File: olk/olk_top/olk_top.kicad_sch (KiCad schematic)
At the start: 64 parts, among them SW0 SWITCH, SW1 SWITCH, SW10 SWITCH, SW11 SWITCH, SW12 SWITCH, SW13 SWITCH, SW14 SWITCH, SW15 SWITCH, SW16 SWITCH, SW17 SWITCH, SW18 SWITCH, SW19 SWITCH, SW2 SWITCH, SW20 SWITCH, SW21 SWITCH, SW22 SWITCH, SW23 SWITCH, SW24 SWITCH, SW25 SWITCH, SW26 SWITCH, SW27 SWITCH, SW28 SWITCH, SW29 SWITCH, SW3 SWITCH, SW30 SWITCH, SW31 SWITCH, SW32 SWITCH, SW33 SWITCH, SW34 SWITCH, SW35 SWITCH, SW36 SWITCH, SW37 SWITCH, SW38 SWITCH, SW39 SWITCH, SW4 SWITCH, SW40 SWITCH, SW41 SWITCH, SW42 SWITCH, SW43 SWITCH, SW44 SWITCH, SW45 SWITCH, SW46 SWITCH, SW47 SWITCH, SW48 SWITCH, SW49 SWITCH, SW5 SWITCH, SW50 SWITCH, SW51 SWITCH, SW52 SWITCH, SW53 SWITCH, SW54 SWITCH, SW55 SWITCH, SW6 SWITCH, SW7 SWITCH, SW8 SWITCH, SW9 SWITCH

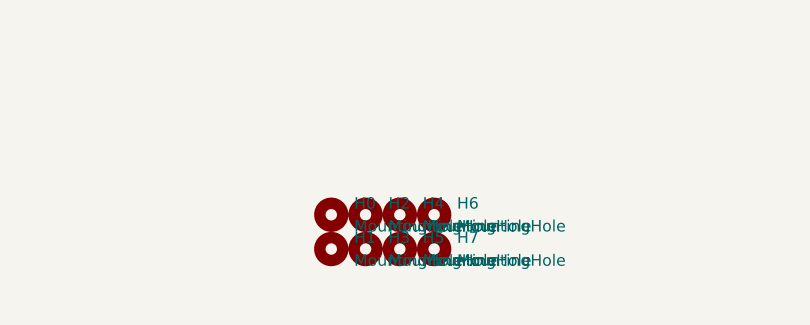
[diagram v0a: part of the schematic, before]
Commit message: Updated the top shape to match the pcb.
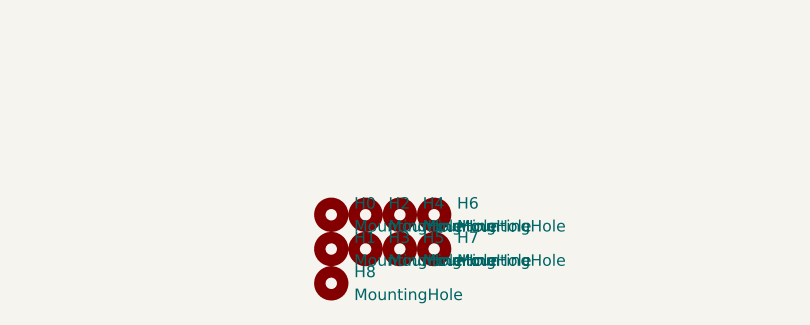
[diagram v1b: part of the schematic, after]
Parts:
- added H8: MountingHole, MountingHole:MountingHole_2.2mm_M2_ISO7380_Pad, symbol Mechanical:MountingHole
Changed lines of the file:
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@@
+	)
+	(symbol
+		(lib_id "Mechanical:MountingHole")
+		(at 119.38 257.81 0)
+		(unit 1)
+		(body_style 1)
+		(exclude_from_sim no)
+		(in_bom yes)
+		(on_board yes)
+		(in_pos_files yes)
+		(dnp no)
+		(fields_autoplaced yes)
+		(property "Reference" "H8"
+			(at 121.92 256.54 0)
+			(show_name no)
+			(do_not_autoplace no)
+			(effects
+				(font
+					(size 1.27 1.27)
+				)
+				(justify left)
+			)
+		)
+		(property "Value" "MountingHole"
+			(at 121.92 259.08 0)
+			(show_name no)
+			(do_not_autoplace no)
+			(effects
+				(font
+					(size 1.27 1.27)
+				)
+				(justify left)
+			)
+		)
+		(property "Footprint" "MountingHole:MountingHole_2.2mm_M2_ISO7380_Pad"
+			(at 119.38 257.81 0)
+			(hide yes)
+			(show_name no)
+			(do_not_autoplace no)
+			(effects
+				(font
+					(size 1.27 1.27)
+				)
+			)
+		)
+		(property "Datasheet" ""
+			(at 119.38 257.81 0)
+			(hide yes)
+			(show_name no)
+			(do_not_autoplace no)
+			(effects
+				(font
+					(size 1.27 1.27)
+				)
+			)
+		)
+		(property "Description" ""
+			(at 119.38 257.81 0)
+			(show_name no)
+			(do_not_autoplace no)
+			(effects
+				(font
+					(size 1.27 1.27)
+				)
+			)
+		)
+		(instances
+			(project "olk_top"
+				(path "/97127b28-60f4-45ff-835e-dccfbc833331"
+					(reference "H8")
+					(unit 1)
+				)
+			)
+		)
 	)
 	(symbol

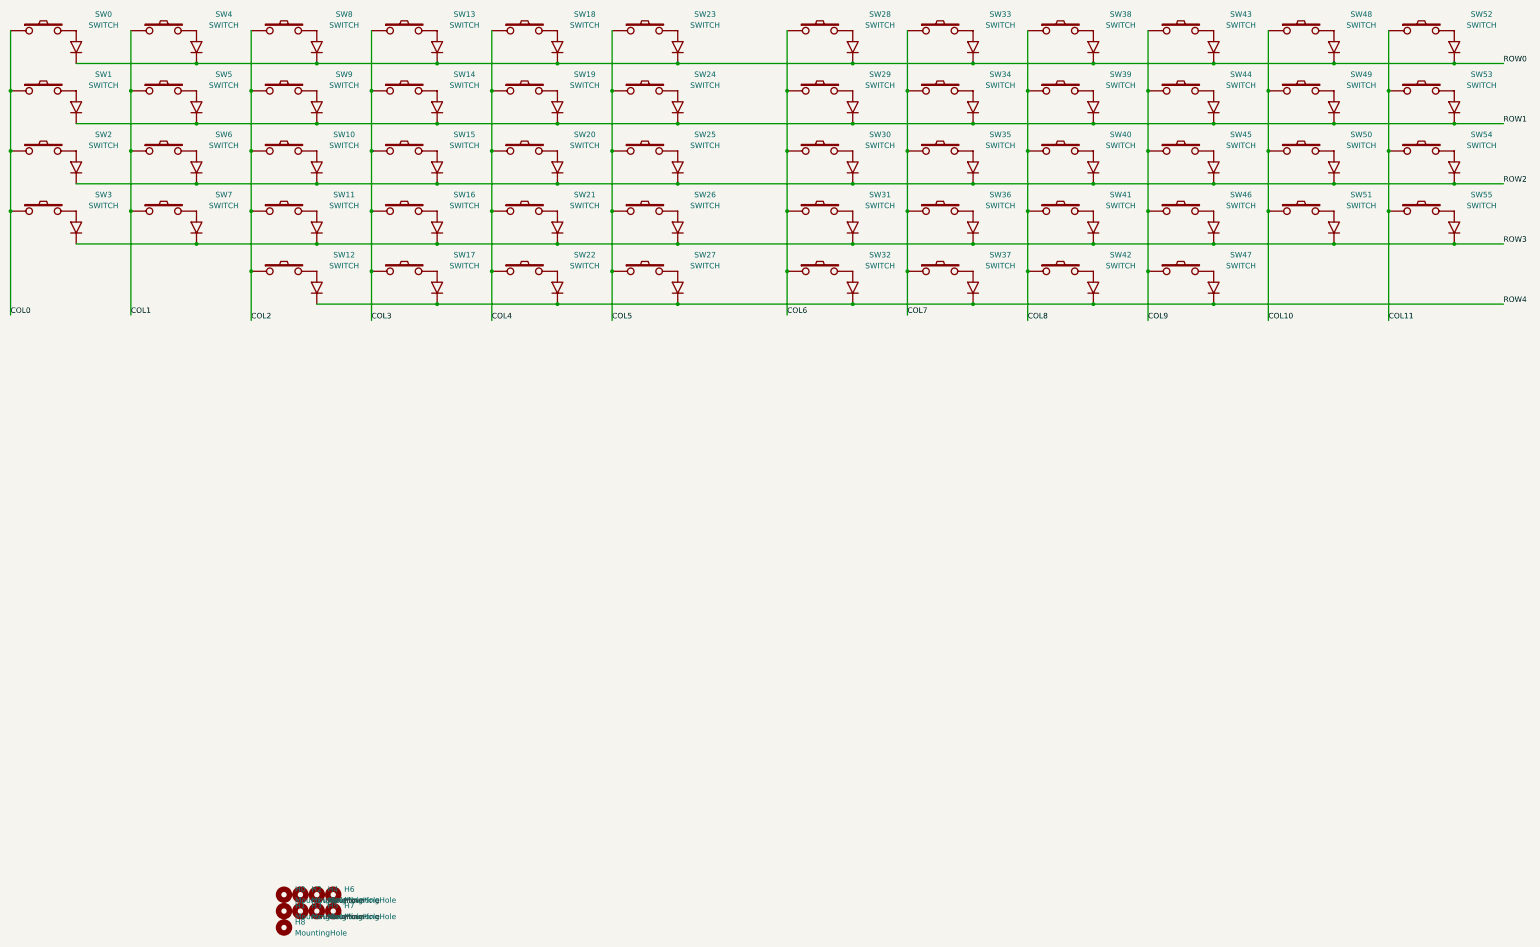
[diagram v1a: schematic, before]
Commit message: Updated olk_top to match the new layout.
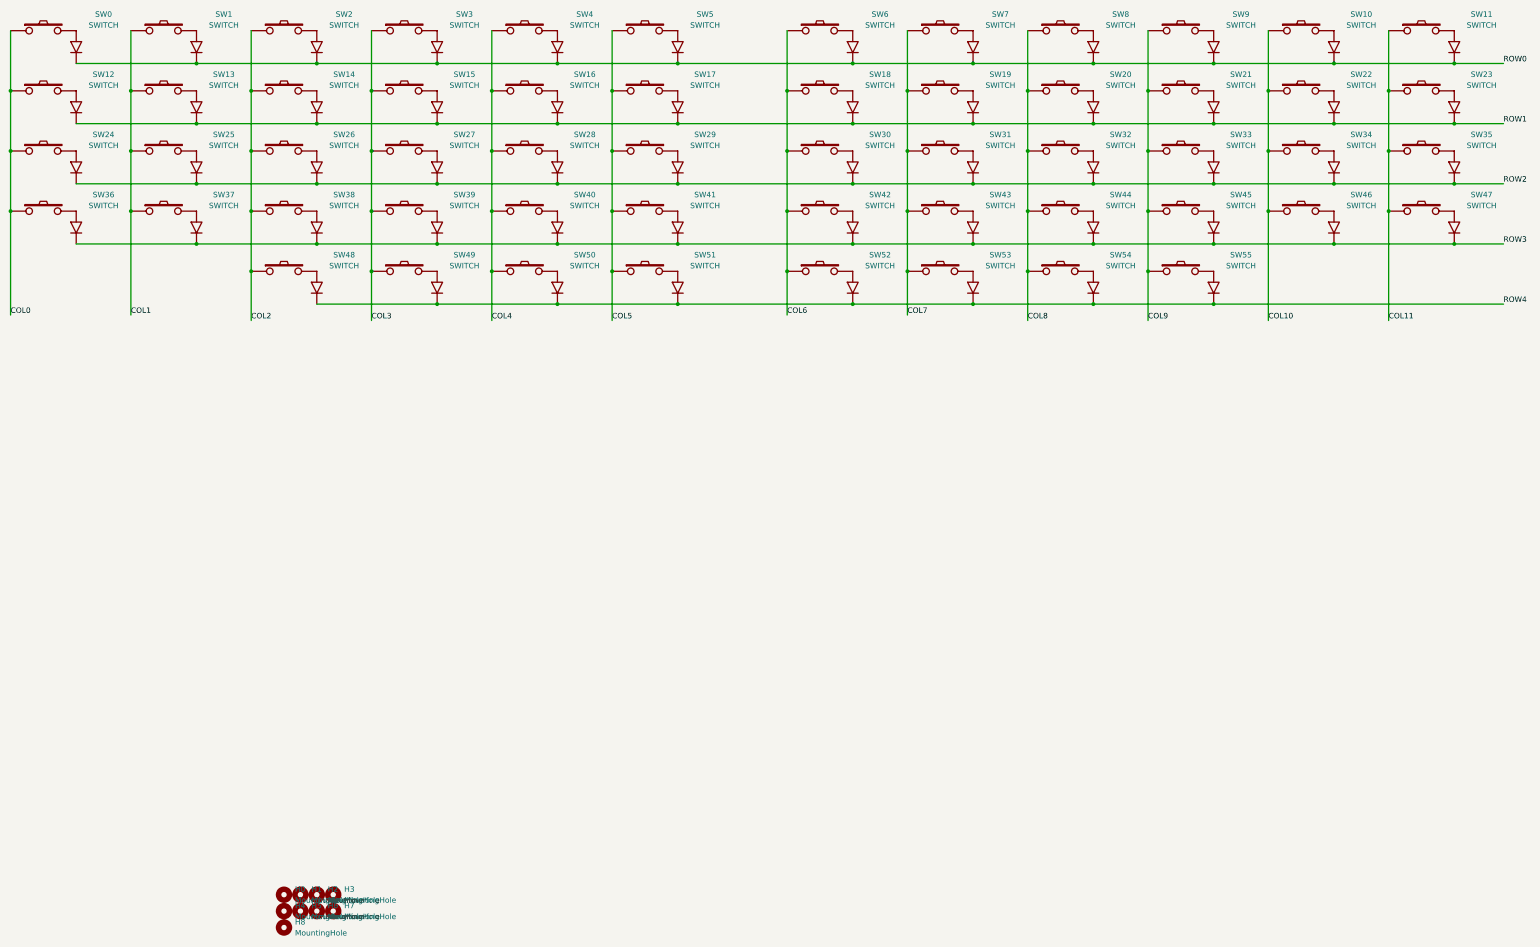
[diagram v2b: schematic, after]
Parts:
- renumbered H2 to H1, H4 to H2, H6 to H3, H1 to H4, H3 to H5, H5 to H6, SW4 to SW1, SW48 to SW10, SW52 to SW11, SW1 to SW12, SW5 to SW13, SW9 to SW14, SW14 to SW15, SW19 to SW16, SW24 to SW17, SW29 to SW18, SW34 to SW19, SW8 to SW2, SW39 to SW20, SW44 to SW21, SW49 to SW22, SW53 to SW23, SW2 to SW24, SW6 to SW25, SW10 to SW26, SW15 to SW27, SW20 to SW28, SW25 to SW29, SW13 to SW3, SW35 to SW31, SW40 to SW32, SW45 to SW33, SW50 to SW34, SW54 to SW35, SW3 to SW36, SW7 to SW37, SW11 to SW38, SW16 to SW39, SW18 to SW4, SW21 to SW40, SW26 to SW41, SW31 to SW42, SW36 to SW43, SW41 to SW44, SW46 to SW45, SW51 to SW46, SW55 to SW47, SW12 to SW48, SW17 to SW49, SW23 to SW5, SW22 to SW50, SW27 to SW51, SW32 to SW52, SW37 to SW53, SW42 to SW54, SW47 to SW55, SW28 to SW6, SW33 to SW7, SW38 to SW8, SW43 to SW9
